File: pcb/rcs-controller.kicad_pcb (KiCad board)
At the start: 2 copper layers, 45.6 x 73 mm, 110 parts, among them J1 00222-32051, J10 0022-232021, J11 Conn_01x03, J2 0022-232021, J3 0022-232041, J4 Screw_Terminal_4_P3.50mm, J5 USB_C_Receptacle_USB2.0_14P, J6 Conn_01x03, J8 00222-32051, J9 Conn_01x03, Q1 SI7465DP-T1-E3, Q2 SI7465DP-T1-E3, Q3 SI7465DP-T1-E3, Q4 PMV45EN2, Q5 PMV45EN2, SW1 SW_Push, SW2 SW_Push, U1 LSM6DSOX, U2 MP26123DR-LF-Z, U3 TPS63070, U4 ESP32-S3-WROOM-1

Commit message: Moved vias off of pads and redid some traces
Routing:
- net +3.3V: track 105.0 -> 103.5 mm
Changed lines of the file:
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@@
 		(tags "2.4 GHz Wi-Fi and Bluetooth module")
 		(property "Reference" "U4"
-			(at 4.4 13.9 0)
+			(at 0 13.95 0)
 			(unlocked yes)
 			(layer "F.SilkS")
@@
 		(tags "capacitor")
 		(property "Reference" "C13"
-			(at 0.2 1.1 270)
+			(at -1.85 0 0)
 			(layer "F.SilkS")
 			(effects
@@
 		(descr "Pin header test point")
 		(property "Reference" "TP1"
-			(at -2.2 -0.1 0)
+			(at -0.7 1.4 0)
 			(layer "F.SilkS")
 			(effects
@@
 		(tags "resistor")
 		(property "Reference" "R1"
-			(at 0.1 1.1 0)
+			(at 1.75 -0.55 0)
 			(layer "F.SilkS")
 			(effects
@@
 		(tags "resistor")
 		(property "Reference" "R15"
-			(at 0.1 -1.2 270)
+			(at 0.5 -1.5 0)
 			(layer "F.SilkS")
 			(effects
@@
 		(tags "LGA NoLead")
 		(property "Reference" "U1"
-			(at -2.2 0 0)
+			(at 2.1 -0.05 0)
 			(layer "F.SilkS")
 			(effects
@@
 		(tags "Diode SMA (DO-214AC)")
 		(property "Reference" "D11"
-			(at -0.2 1.3 0)
+			(at 2.85 -2.15 0)
 			(layer "F.SilkS")
 			(effects
@@
 		(tags "LED")
 		(property "Reference" "D7"
-			(at -2.3 -0.3 180)
+			(at 1.75 0 180)
 			(layer "F.SilkS")
 			(effects
@@
 		(descr "Pin header test point")
 		(property "Reference" "TP32"
-			(at -2.1 -0.8 0)
+			(at -0.95 1.5 0)
 			(layer "F.SilkS")
 			(effects
@@
 		(tags "resistor")
 		(property "Reference" "R5"
-			(at -0.7 -1.3 0)
+			(at -1.7 0 0)
 			(layer "F.SilkS")
 			(effects
@@
 		(tags "LED")
 		(property "Reference" "D2"
-			(at -1.9 0.33 0)
+			(at 1.7 -0.22 0)
 			(layer "F.SilkS")
 			(effects
@@
 		(tags "resistor")
 		(property "Reference" "R33"
-			(at 0 -1.43 90)
+			(at 0 -1.5 180)
 			(layer "F.SilkS")
 			(effects
 				(font
-					(size 1 1)
-					(thickness 0.15)
+					(size 0.5 0.5)
+					(thickness 0.125)
 				)
 			)
@@
 		(tags "resistor")
 		(property "Reference" "R3"
-			(at -0.075 -1.1 270)
+			(at -1.575 -0.1 0)
 			(layer "F.SilkS")
 			(effects
@@
 		(tags "connector Molex KK-254 vertical")
 		(property "Reference" "J11"
-			(at 3.58 -3.9 0)
+			(at 6.93 2.5 0)
 			(unlocked yes)
 			(layer "F.SilkS")
@@
 		(at 128.4 110 90)
 		(property "Reference" "U3"
-			(at 1.1 2.4 0)
+			(at 2 -0.65 0)
 			(unlocked yes)
 			(layer "F.SilkS")
@@
 		(tags "Diode SMA (DO-214AC)")
 		(property "Reference" "D13"
-			(at -4.57 -0.175 0)
+			(at -0.15 2.425 0)
 			(layer "F.SilkS")
 			(effects
@@
 		(tags "Diode SMA (DO-214AC)")
 		(property "Reference" "D10"
-			(at 2.9 1.7 0)
+			(at 3.1 -1.4 0)
 			(layer "F.SilkS")
 			(effects
@@
 		(tags "resistor")
 		(property "Reference" "R35"
-			(at 1.8 -1.8 0)
+			(at 0.2 -1.65 0)
 			(layer "F.SilkS")
 			(effects
@@
 	)
 	(via
-		(at 128.4 137.6)
+		(at 126.75 137.6)
 		(size 0.508)
 		(drill 0.254)
@@
 		(layer "F.Cu")
 		(net "+3.3V")
-	)
-	(segment
-		(start 127.625 107.2)
-		(end 127.625 105.7)
-		(width 0.5)
-		(layer "F.Cu")
-		(net "+3.3V")

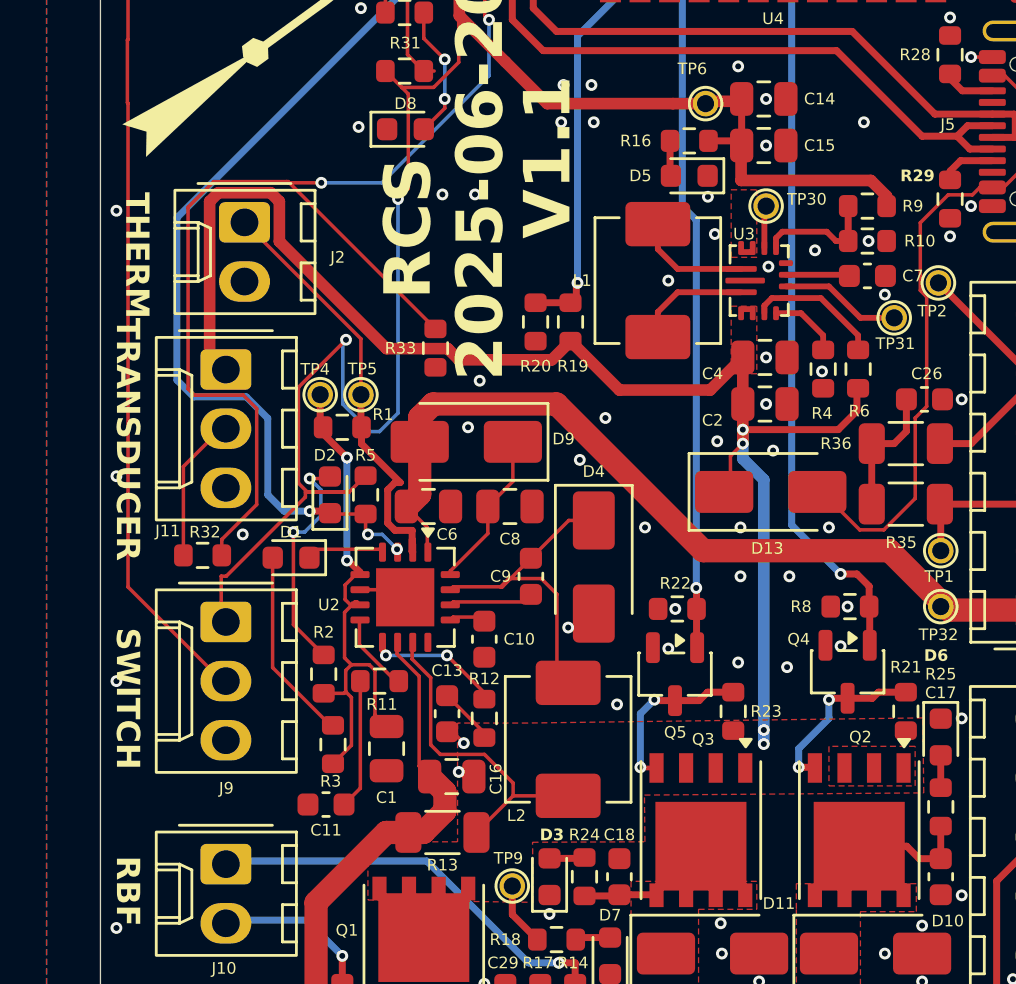
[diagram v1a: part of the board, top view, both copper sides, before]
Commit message: Rerouted traces to clean up
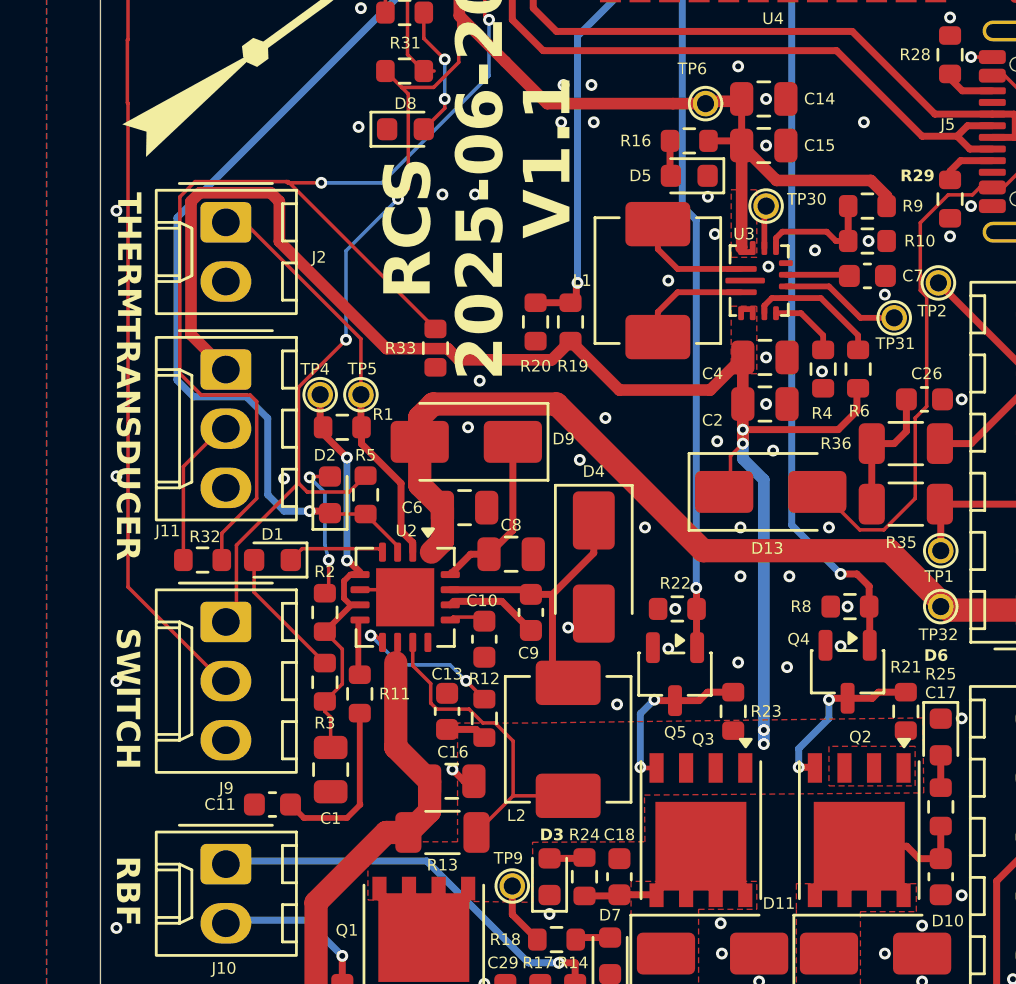
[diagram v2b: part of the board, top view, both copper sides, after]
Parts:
- moved R3 2.70 mm to (109.8, 127.2)
- moved R2 2.65 mm to (109.8, 124.2)
- moved C1 2.56 mm to (110.0, 131.0)
- moved C11 2.30 mm to (107.5, 132.5)
- moved C8 2.05 mm to (117.8, 121.8)
- moved C6 1.55 mm to (115.8, 119.8)
- moved C9 1.55 mm to (118.6, 124.2)
- moved R11 1.01 mm to (111.2, 127.8), turned to -90 degrees
- moved D1 0.81 mm to (107.5, 122.0)
- moved J2 0.80 mm to (105.5, 107.5)
- moved R32 0.20 mm to (104.5, 122.0)
- moved C16 0.20 mm to (115.2, 131.5)
- moved C13 0.10 mm to (115.0, 128.5), turned to 90 degrees
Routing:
- net +3.3V: track 103.5 -> 97.2 mm
- net /Power/VREF33: track 23.4 -> 18.4 mm
- net Net-(D2-A): track 9.99 -> 6.34 mm
- net Net-(D1-A): track 8.34 -> 6.04 mm
- net VBUS: track 65.9 -> 67.8 mm
- net Net-(C11-Pad1): track 5.59 -> 7.42 mm
- net +BATT: track 21.3 -> 19.7 mm
- net Net-(U2-COMPI): track 5.81 -> 6.95 mm
- net Net-(D1-K): track 3.52 -> 4.59 mm
- net Net-(U4-IO6): track 59.4 -> 60.4 mm
- net Net-(U2-COMPV): track 3.41 -> 2.46 mm
- net Net-(J2-Pin_1): track 18.7 -> 18.0 mm
- net Net-(C13-Pad1): track 2.46 -> 1.74 mm
- net Net-(D4-K): track 14.2 -> 13.6 mm
- net Net-(D9-K): track 6.81 -> 7.42 mm
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
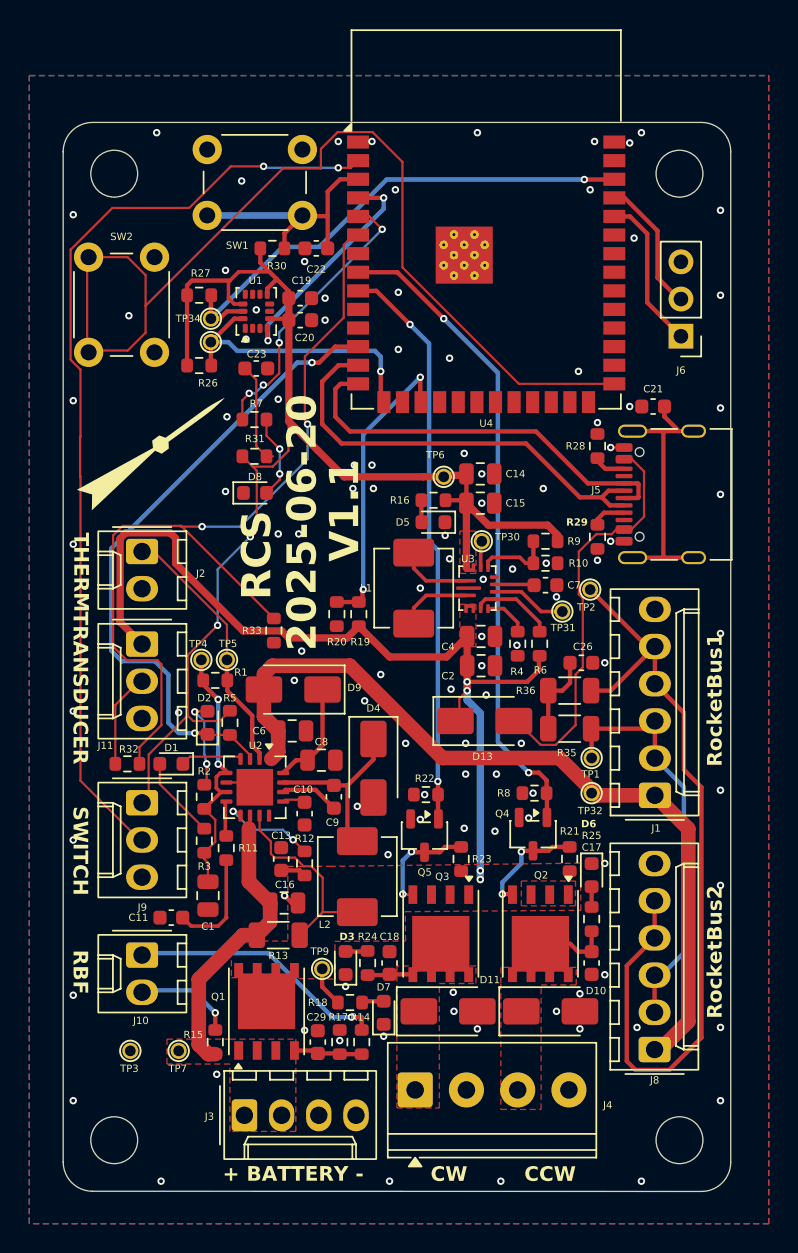
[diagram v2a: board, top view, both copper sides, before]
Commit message: Cleaned up traces and min trace width is now .3 mm
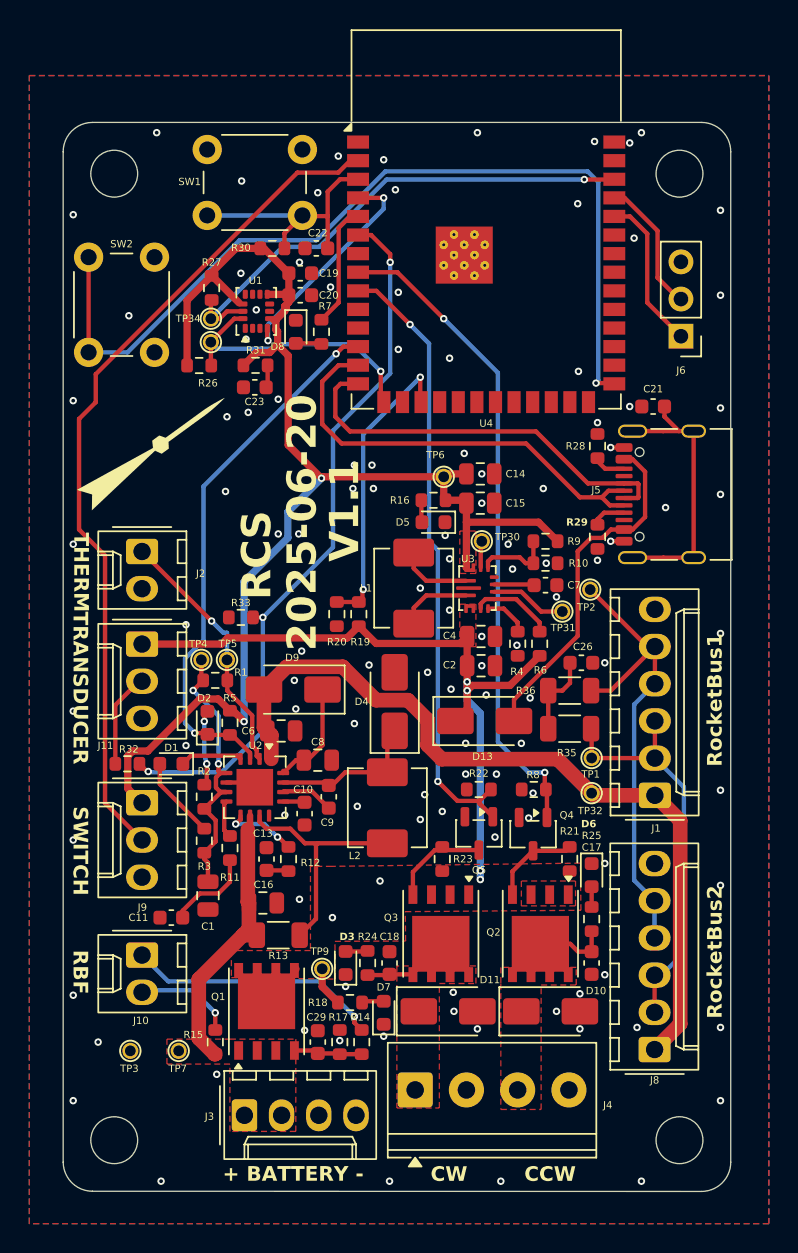
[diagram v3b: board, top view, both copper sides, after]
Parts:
- moved D8 11.3 mm to (116.0, 92.5), turned to -90 degrees
- moved R7 7.54 mm to (117.8, 92.5), turned to -90 degrees
- moved R31 6.21 mm to (113.2, 94.8)
- moved L2 5.13 mm to (122.2, 125.0)
- moved D4 4.78 mm to (122.8, 117.8), turned to 90 degrees
- moved Q5 3.72 mm to (128.5, 126.8)
- moved R22 3.63 mm to (128.5, 123.8)
- moved R33 2.42 mm to (112.2, 112.0), turned to 0 degrees
- moved C19 1.70 mm to (116.3, 88.5)
- moved C20 1.70 mm to (116.3, 90.0)
- moved C16 1.45 mm to (113.8, 131.5)
- moved C23 1.29 mm to (113.2, 96.3), turned to 180 degrees
- moved R23 1.29 mm to (126.0, 128.5)
- moved R12 1.14 mm to (115.5, 128.5)
- moved C13 1.00 mm to (114.0, 128.5)
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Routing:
- net CANL: track 57.9 -> 33.0 mm
- net VBUS: track 67.8 -> 53.9 mm
- net Net-(U4-IO5): track 19.6 -> 8.40 mm, vias 4 -> 0
- net Net-(U4-IO6): track 60.4 -> 49.4 mm, vias 2 -> 3
- net UMB_~{ON}: track 44.2 -> 36.9 mm
- net Net-(J9-Pin_2): track 64.5 -> 58.0 mm, vias 2 -> 0
- net Net-(U4-IO0): track 68.2 -> 61.8 mm, vias 0 -> 1
- net Net-(C23-Pad1): track 6.75 -> 1.54 mm
- net +5V: track 27.8 -> 23.8 mm
- net Net-(D8-A): track 5.76 -> 1.77 mm, vias 2 -> 0
- net Net-(Q5-G): track 39.0 -> 42.4 mm
- net +3.3V: track 97.2 -> 94.1 mm
- net Net-(D4-K): track 13.6 -> 10.6 mm
- net Net-(U2-CSP): track 14.1 -> 16.5 mm
- net Net-(U2-COMPI): track 6.95 -> 4.96 mm
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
